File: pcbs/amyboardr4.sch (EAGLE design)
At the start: 129 parts, among them J1 52601-G10-8LF, M13 M2.5, M14 M2.5, M15 M2.5, M16 M2.5, Q2 S8050, Q5 S8050, U1 PCM9211PT, U13 HX3608, U15 H11L1SR2M, U16 SPX3819, U2 ESP32­S2­SOLO, Y1 ABM10W-22.5792MHZ-8-K1Z-T3

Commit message: .
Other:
- note added: "NOTES/TODO: - MabeeDAC to provide VOUT0 and VOUT1 - NC/GND unused pins - 12V -> 5V regulator for modular port - Confirm VOUT / VPWR / 3v3 / 5v / 12V"
- note removed: "NOTES/TODO: - RXGND? Is it just GND? - MabeeDAC to provide VOUT0 and VOUT1 - Expanded header with 5V, extra GPIOs, UART - I2C main grove/mabee connector as well ?? - NC/GND unused pins - Confirm power / VPWR / 3v3 / 5v - Remove/test single USB NATIVE port"
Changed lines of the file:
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@@
 <text x="192.786" y="113.538" size="5.08" layer="97">HEADERS</text>
 <text x="294.64" y="190.5" size="3.81" layer="97">NOTES/TODO:
-- RXGND? Is it just GND?
 - MabeeDAC to provide VOUT0 and VOUT1
-- Expanded header with 5V, extra GPIOs, UART
-- I2C main grove/mabee connector as well ??
 - NC/GND unused pins
-- Confirm power / VPWR / 3v3 / 5v
-- Remove/test single USB NATIVE port</text>
+- 12V -&gt; 5V regulator for modular port
+- Confirm VOUT / VPWR / 3v3 / 5v / 12V
+</text>
 <text x="129.54" y="-54.61" size="5.08" layer="97">TF Card</text>
 <text x="193.548" y="-73.406" size="1.778" layer="97">D3</text>

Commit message: moving around
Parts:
- Y1: value ABM10W-22.5792MHZ-8-K1Z-T3 -> 22.5792MHZ
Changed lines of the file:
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@@
 <part name="R97" library="A9G" deviceset="DISCRETE_R*" device="-0603" value="88.7K"/>
 <part name="R98" library="A9G" deviceset="DISCRETE_R*" device="-0603" value="12K"/>
-<part name="Y1" library="ABM10W-22.5792MHZ-8-K1Z-T3" deviceset="ABM10W-22.5792MHZ-8-K1Z-T3" device=""/>
+<part name="Y1" library="ABM10W-22.5792MHZ-8-K1Z-T3" deviceset="ABM10W-22.5792MHZ-8-K1Z-T3" device="" value="22.5792MHZ"/>
 <part name="C1" library="Discrete-new" deviceset="CAP" device="-0603" value="0.1uF"/>
 <part name="C2" library="microbuilder" deviceset="CAP_ELECTROLYTIC" device="PANASONIC_C" value="10uF"/>

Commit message: r4 with top jacks
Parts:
- removed M13, M14, M15, M16: M2.5, sale:M2.5
- removed SPDIF_OUT: SJ1-3543, SJ1-3543:SJ1-3543
- added U$16: NV-PJ3410_STEREO, PJ3410_sockets:NV-PJ3410_STEREO
- CV_IN1, CV_IN2, CV_OUT1, CV_OUT2, LINE_IN, LINE_OUT, MIDI_IN, MIDI_OUT, SPDIF_IN: value SJ1-3543 -> NV-PJ3410_STEREO; device SJ1-3543:SJ1-3543 -> PJ3410_sockets:NV-PJ3410_STEREO
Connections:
- removed net N$15: CV_OUT2.1
- net AGND: now also LINE_IN.EARTH, LINE_OUT.EARTH; no longer LINE_IN.1, LINE_OUT.1
- net GND: now also CV_IN1.EARTH, CV_OUT1.EARTH, CV_OUT2.EARTH, MIDI_IN.EARTH, MIDI_OUT.EARTH, SPDIF_IN.EARTH, U$16.EARTH; no longer CV_IN1.1, CV_IN2.1, CV_OUT1.1, M13.P$1, M14.P$1, M15.P$1, M16.P$1, MIDI_IN.1, MIDI_OUT.1, SPDIF_IN.1, SPDIF_OUT.1
- net LIN: now also LINE_IN.TIP; no longer LINE_IN.2
- net LOUT: now also LINE_OUT.TIP; no longer LINE_OUT.2
- net MABEEDAC_VOUT0: now also CV_OUT1.TIP; no longer CV_OUT1.2
- net MABEEDAC_VOUT1: now also CV_OUT2.TIP; no longer CV_OUT2.2
- net N$10: now also SPDIF_IN.RING; no longer SPDIF_IN.3
- net N$11: now also CV_OUT1.RING; no longer CV_OUT1.3
- net N$12: now also CV_OUT2.RING; no longer CV_OUT2.3
- net N$13: now also CV_IN1.RING; no longer CV_IN1.3
- net N$14: now also CV_IN2.RING; no longer CV_IN2.3
- net N$17: now also CV_IN1.TIP; no longer CV_IN1.2
- net N$19: now also CV_IN2.TIP; no longer CV_IN2.2
- net N$55: now also MIDI_IN.TIP; no longer MIDI_IN.2
- net N$56: now also MIDI_IN.RING; no longer MIDI_IN.3
- net N$58: now also MIDI_OUT.TIP; no longer MIDI_OUT.2
- net N$59: now also MIDI_OUT.RING; no longer MIDI_OUT.3
- net N$9: now also U$16.RING; no longer SPDIF_OUT.3
- net RIN: now also LINE_IN.RING; no longer LINE_IN.3
- net ROUT: now also LINE_OUT.RING; no longer LINE_OUT.3
- net SPDIFIN_SIGNAL: now also SPDIF_IN.TIP; no longer SPDIF_IN.2
- net SPDIFOUT_SIGNAL: now also U$16.TIP; no longer SPDIF_OUT.2

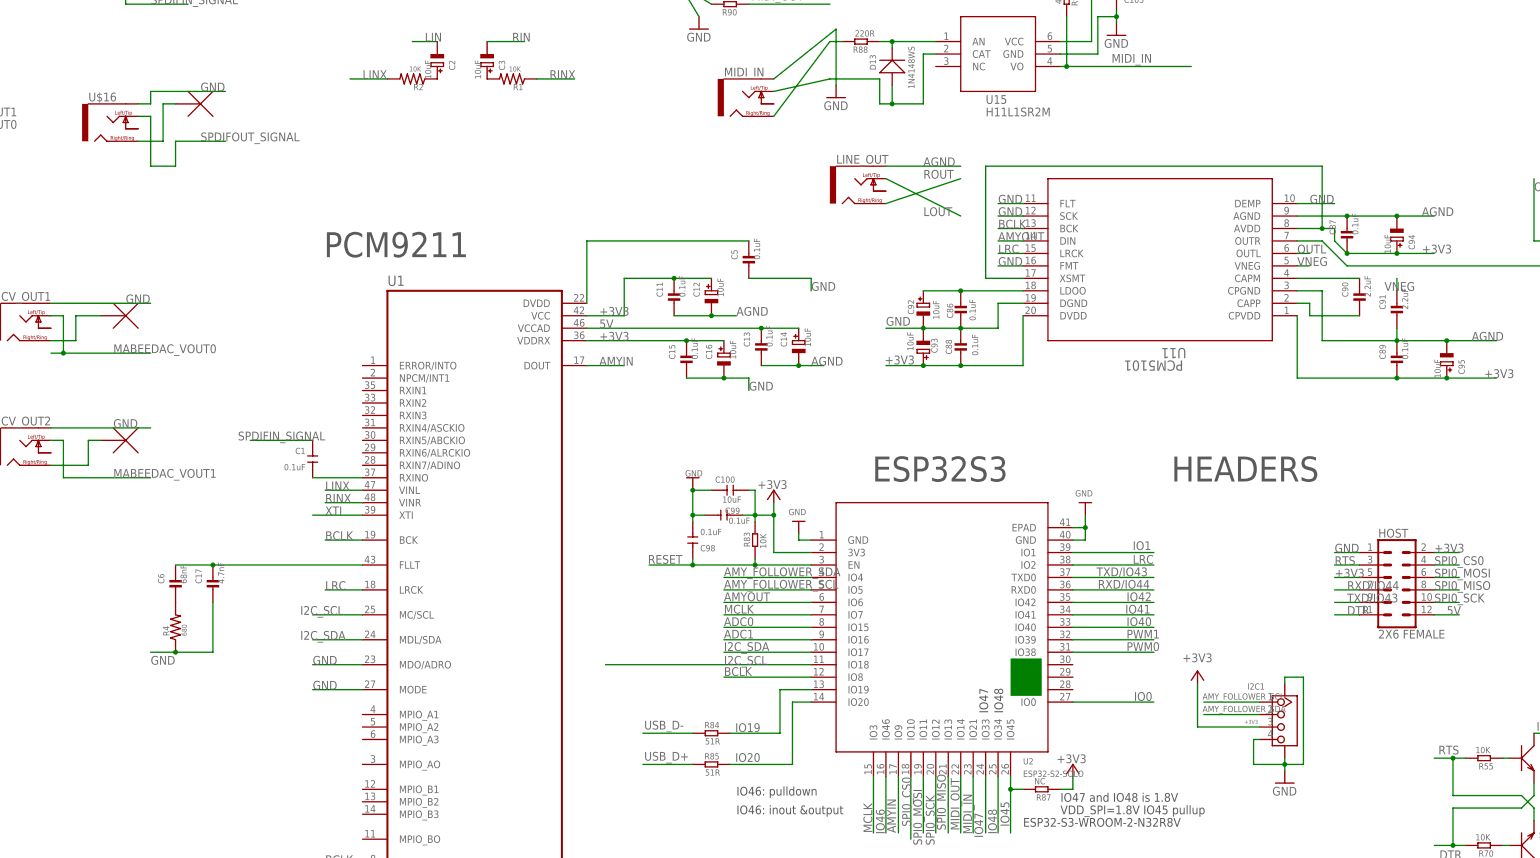
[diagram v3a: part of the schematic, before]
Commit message: moving jacks together on bottom
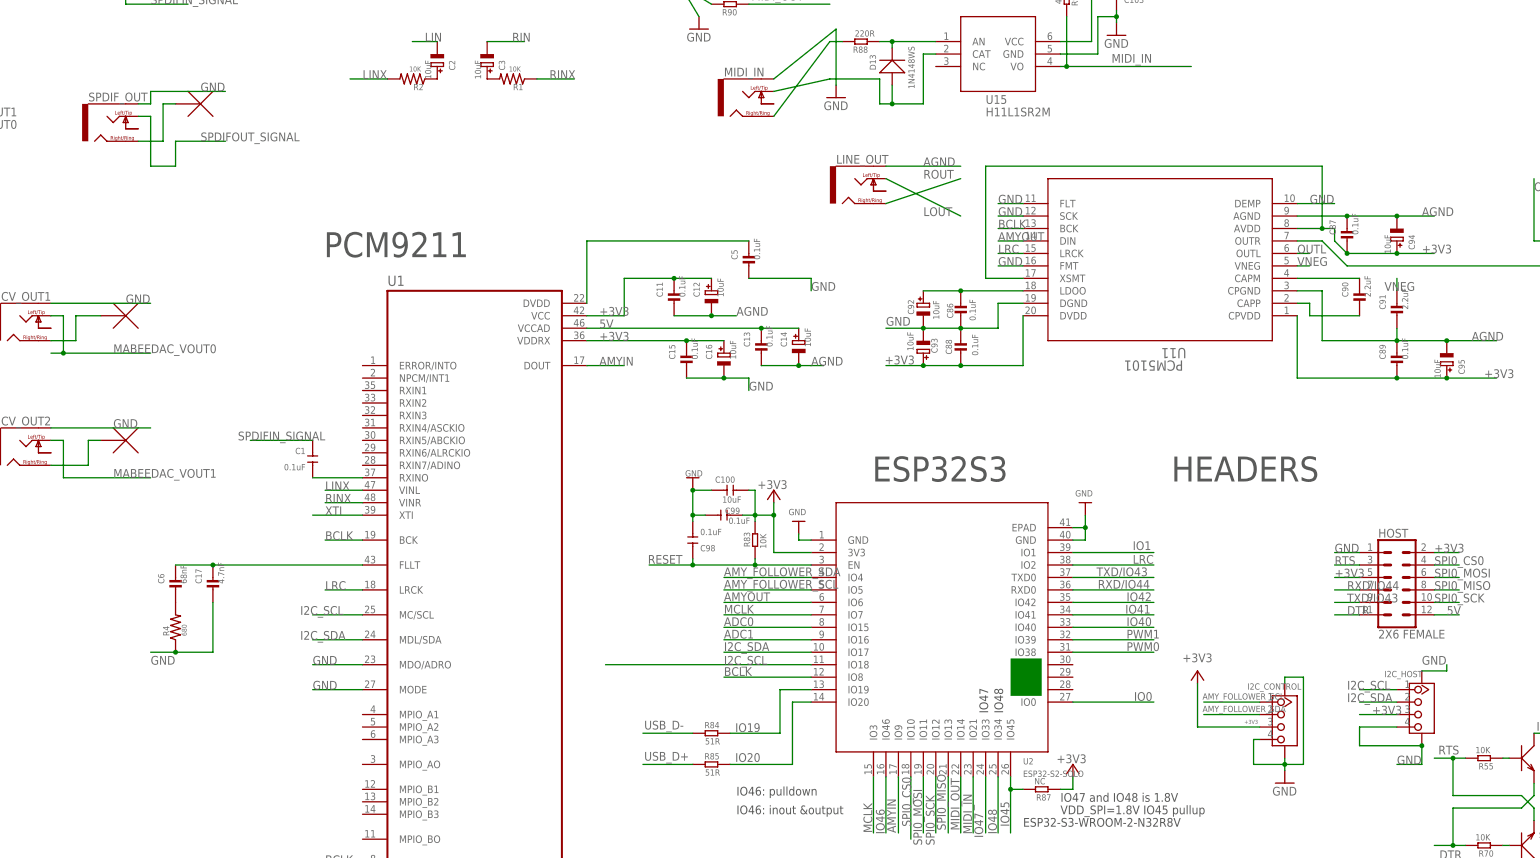
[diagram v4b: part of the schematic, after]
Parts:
- added I2C_HOST: (no value), Connector-new:GROVE-CONNECTOR-SMD'90D'
- renumbered I2C1 to I2C_CONTROL, U$16 to SPDIF_OUT
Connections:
- net +3V3: now also I2C_HOST.3
- net GND: now also I2C_HOST.4, I2C_HOST.SS1, I2C_HOST.SS2
- net I2C_SCL: now also I2C_HOST.1
- net I2C_SDA: now also I2C_HOST.2
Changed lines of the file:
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@@
 <parts>
 <part name="U1" library="PCM9211PT" deviceset="PCM9211PT" device=""/>
-<part name="I2C1" library="Connector-new" deviceset="GROVE-CONNECTOR-SMD" device="'90D'"/>
+<part name="I2C_CONTROL" library="Connector-new" deviceset="GROVE-CONNECTOR-SMD" device="'90D'"/>
 <part name="+3V11" library="supply1" deviceset="+3V3" device=""/>
 <part name="GND86" library="supply1" deviceset="GND" device=""/>
@@
 <part name="CV_OUT2" library="PJ3410_sockets" deviceset="NV-PJ3410_STEREO" device=""/>
 <part name="SPDIF_IN" library="PJ3410_sockets" deviceset="NV-PJ3410_STEREO" device=""/>
-<part name="U$16" library="PJ3410_sockets" deviceset="NV-PJ3410_STEREO" device=""/>
+<part name="SPDIF_OUT" library="PJ3410_sockets" deviceset="NV-PJ3410_STEREO" device=""/>
+<part name="I2C_HOST" library="Connector-new" deviceset="GROVE-CONNECTOR-SMD" device="'90D'"/>
 </parts>
 <sheets>
@@
 <attribute name="VALUE" x="33.02" y="-29.4" size="2.0828" layer="96" ratio="10" rot="SR0"/>
 </instance>
-<instance part="I2C1" gate="G$1" x="215.9" y="64.77" smashed="yes">
+<instance part="I2C_CONTROL" gate="G$1" x="215.9" y="64.77" smashed="yes">
 <attribute name="NAME" x="208.28" y="71.12" size="1.27" layer="95" ratio="10"/>
 <attribute name="VALUE" x="217.17" y="71.12" size="1.27" layer="96" ratio="10"/>
@@
 <attribute name="NAME" x="-33.02" y="221.488" size="1.778" layer="95"/>
 </instance>
-<instance part="U$16" gate="G$1" x="-22.86" y="185.42" smashed="yes">
+<instance part="SPDIF_OUT" gate="G$1" x="-22.86" y="185.42" smashed="yes">
 <attribute name="NAME" x="-27.94" y="191.008" size="1.778" layer="95"/>
+</instance>
+<instance part="I2C_HOST" gate="G$1" x="243.84" y="67.31" smashed="yes">
+<attribute name="NAME" x="236.22" y="73.66" size="1.27" layer="95" ratio="10"/>
+<attribute name="VALUE" x="245.11" y="73.66" size="1.27" layer="96" ratio="10"/>
 </instance>
 </instances>
@@
 <net name="GND" class="0">
 <segment>
-<pinref part="I2C1" gate="G$1" pin="SS2"/>
+<pinref part="I2C_CONTROL" gate="G$1" pin="SS2"/>
 <wire x1="215.9" y1="57.15" x2="215.9" y2="55.88" width="0.1524" layer="91"/>
-<pinref part="I2C1" gate="G$1" pin="SS1"/>
+<pinref part="I2C_CONTROL" gate="G$1" pin="SS1"/>
 <wire x1="215.9" y1="55.88" x2="215.9" y2="54.61" width="0.1524" layer="91"/>
 <wire x1="215.9" y1="72.39" x2="215.9" y2="73.66" width="0.1524" layer="91"/>
@@
 <wire x1="219.71" y1="55.88" x2="215.9" y2="55.88" width="0.1524" layer="91"/>
 <junction x="215.9" y="55.88"/>
-<pinref part="I2C1" gate="G$1" pin="4"/>
+<pinref part="I2C_CONTROL" gate="G$1" pin="4"/>
 <wire x1="210.82" y1="60.96" x2="209.55" y2="60.96" width="0.1524" layer="91"/>
 <wire x1="209.55" y1="60.96" x2="209.55" y2="55.88" width="0.1524" layer="91"/>
@@
 <label x="-5.08" y="193.04" size="1.778" layer="95"/>
 <wire x1="-15.24" y1="193.04" x2="-15.24" y2="190.5" width="0.1524" layer="91"/>
-<pinref part="U$16" gate="G$1" pin="EARTH"/>
+<pinref part="SPDIF_OUT" gate="G$1" pin="EARTH"/>
 <wire x1="-15.24" y1="190.5" x2="-17.78" y2="190.5" width="0.1524" layer="91"/>
 </segment>
@@
 <label x="-22.86" y="124.46" size="1.778" layer="95"/>
 </segment>
+<segment>
+<pinref part="I2C_HOST" gate="G$1" pin="SS1"/>
+<wire x1="243.84" y1="74.93" x2="248.92" y2="74.93" width="0.1524" layer="91"/>
+<wire x1="248.92" y1="74.93" x2="248.92" y2="76.2" width="0.1524" layer="91"/>
+<label x="243.84" y="76.2" size="1.778" layer="95"/>
+</segment>
+<segment>
+<pinref part="I2C_HOST" gate="G$1" pin="4"/>
+<wire x1="238.76" y1="63.5" x2="231.14" y2="63.5" width="0.1524" layer="91"/>
+<wire x1="231.14" y1="63.5" x2="231.14" y2="59.69" width="0.1524" layer="91"/>
+<pinref part="I2C_HOST" gate="G$1" pin="SS2"/>
+<wire x1="231.14" y1="59.69" x2="243.84" y2="59.69" width="0.1524" layer="91"/>
+<wire x1="243.84" y1="59.69" x2="243.84" y2="55.88" width="0.1524" layer="91"/>
+<wire x1="243.84" y1="55.88" x2="238.76" y2="55.88" width="0.1524" layer="91"/>
+<junction x="243.84" y="59.69"/>
+<label x="238.76" y="55.88" size="1.778" layer="95"/>
+</segment>
 </net>
 <net name="+3V3" class="0">
 <segment>
 <label x="207.645" y="64.135" size="0.8128" layer="95"/>
-<pinref part="I2C1" gate="G$1" pin="3"/>
+<pinref part="I2C_CONTROL" gate="G$1" pin="3"/>
 <wire x1="198.12" y1="63.5" x2="210.82" y2="63.5" width="0.1524" layer="91"/>
 <wire x1="198.12" y1="72.39" x2="198.12" y2="63.5" width="0.1524" layer="91"/>
@@
 <label x="226.06" y="93.98" size="1.778" layer="95"/>
 </segment>
+<segment>
+<pinref part="I2C_HOST" gate="G$1" pin="3"/>
+<wire x1="238.76" y1="66.04" x2="231.14" y2="66.04" width="0.1524" layer="91"/>
+<label x="233.68" y="66.04" size="1.778" layer="95"/>
+</segment>
 </net>
 <net name="RESET" class="0">
@@
 </segment>
 <segment>
-<pinref part="I2C1" gate="G$1" pin="2"/>
+<pinref part="I2C_CONTROL" gate="G$1" pin="2"/>
 <wire x1="210.82" y1="66.04" x2="199.39" y2="66.04" width="0.1524" layer="91"/>
 <label x="199.136" y="66.548" size="1.27" layer="95" ratio="5"/>
@@
 <wire x1="27.94" y1="86.36" x2="17.78" y2="86.36" width="0.1524" layer="91"/>
 <label x="15.24" y="86.36" size="1.778" layer="95"/>
+</segment>
+<segment>
+<pinref part="I2C_HOST" gate="G$1" pin="1"/>
+<wire x1="238.76" y1="71.12" x2="231.14" y2="71.12" width="0.1524" layer="91"/>
+<label x="228.6" y="71.12" size="1.778" layer="95"/>
 </segment>
 </net>
@@
 <label x="15.24" y="81.28" size="1.778" layer="95"/>
 </segment>
+<segment>
+<pinref part="I2C_HOST" gate="G$1" pin="2"/>
+<wire x1="238.76" y1="68.58" x2="231.14" y2="68.58" width="0.1524" layer="91"/>
+<label x="228.6" y="68.58" size="1.778" layer="95"/>
+</segment>
 </net>
 <net name="N$1" class="0">
@@
 <wire x1="-10.16" y1="177.8" x2="-15.24" y2="177.8" width="0.1524" layer="91"/>
 <wire x1="-15.24" y1="177.8" x2="-15.24" y2="187.96" width="0.1524" layer="91"/>
-<pinref part="U$16" gate="G$1" pin="TIP"/>
+<pinref part="SPDIF_OUT" gate="G$1" pin="TIP"/>
 <wire x1="-15.24" y1="187.96" x2="-17.78" y2="187.96" width="0.1524" layer="91"/>
 </segment>
@@
 </segment>
 <segment>
-<pinref part="I2C1" gate="G$1" pin="1"/>
+<pinref part="I2C_CONTROL" gate="G$1" pin="1"/>
 <wire x1="210.82" y1="68.58" x2="199.39" y2="68.58" width="0.1524" layer="91"/>
 <label x="199.136" y="69.088" size="1.27" layer="95"/>
@@
 <wire x1="-10.16" y1="190.5" x2="-12.7" y2="190.5" width="0.1524" layer="91"/>
 <wire x1="-12.7" y1="190.5" x2="-12.7" y2="182.88" width="0.1524" layer="91"/>
-<pinref part="U$16" gate="G$1" pin="RING"/>
+<pinref part="SPDIF_OUT" gate="G$1" pin="RING"/>
 <wire x1="-12.7" y1="182.88" x2="-17.78" y2="182.88" width="0.1524" layer="91"/>
 </segment>
